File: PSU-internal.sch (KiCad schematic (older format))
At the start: 52 parts, among them Q3 BD241A

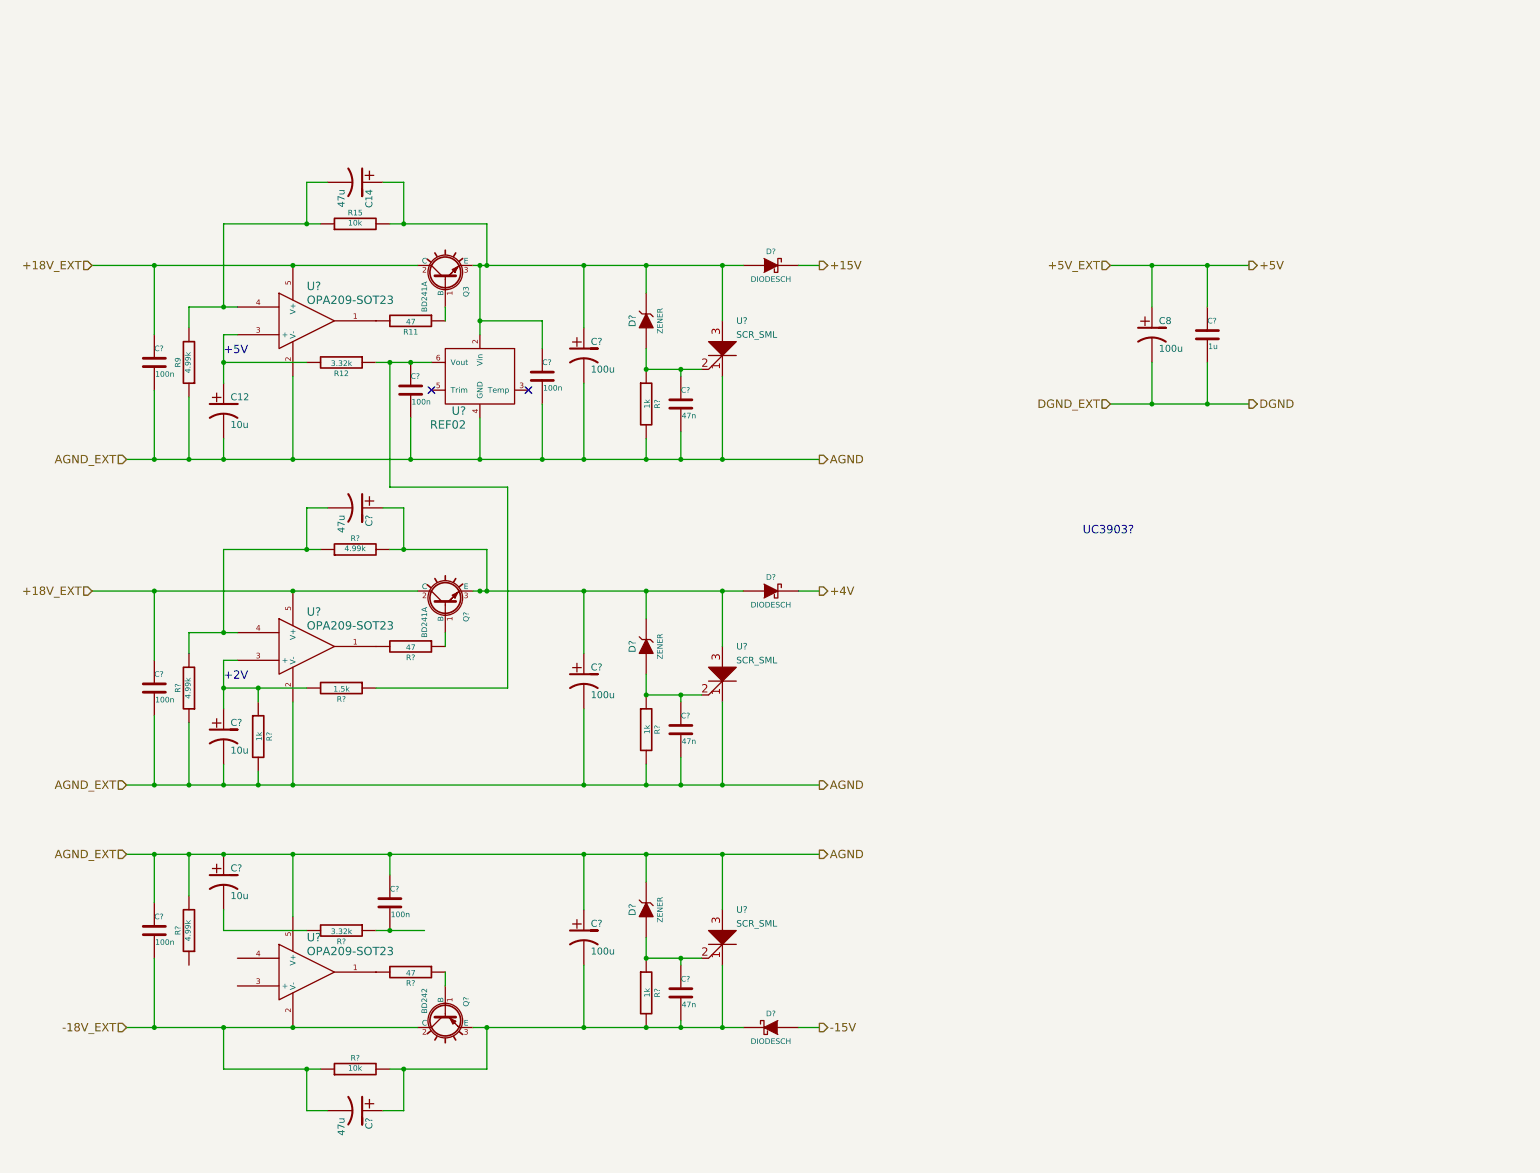
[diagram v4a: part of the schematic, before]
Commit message: Cleaned up the internal PSU a bit.
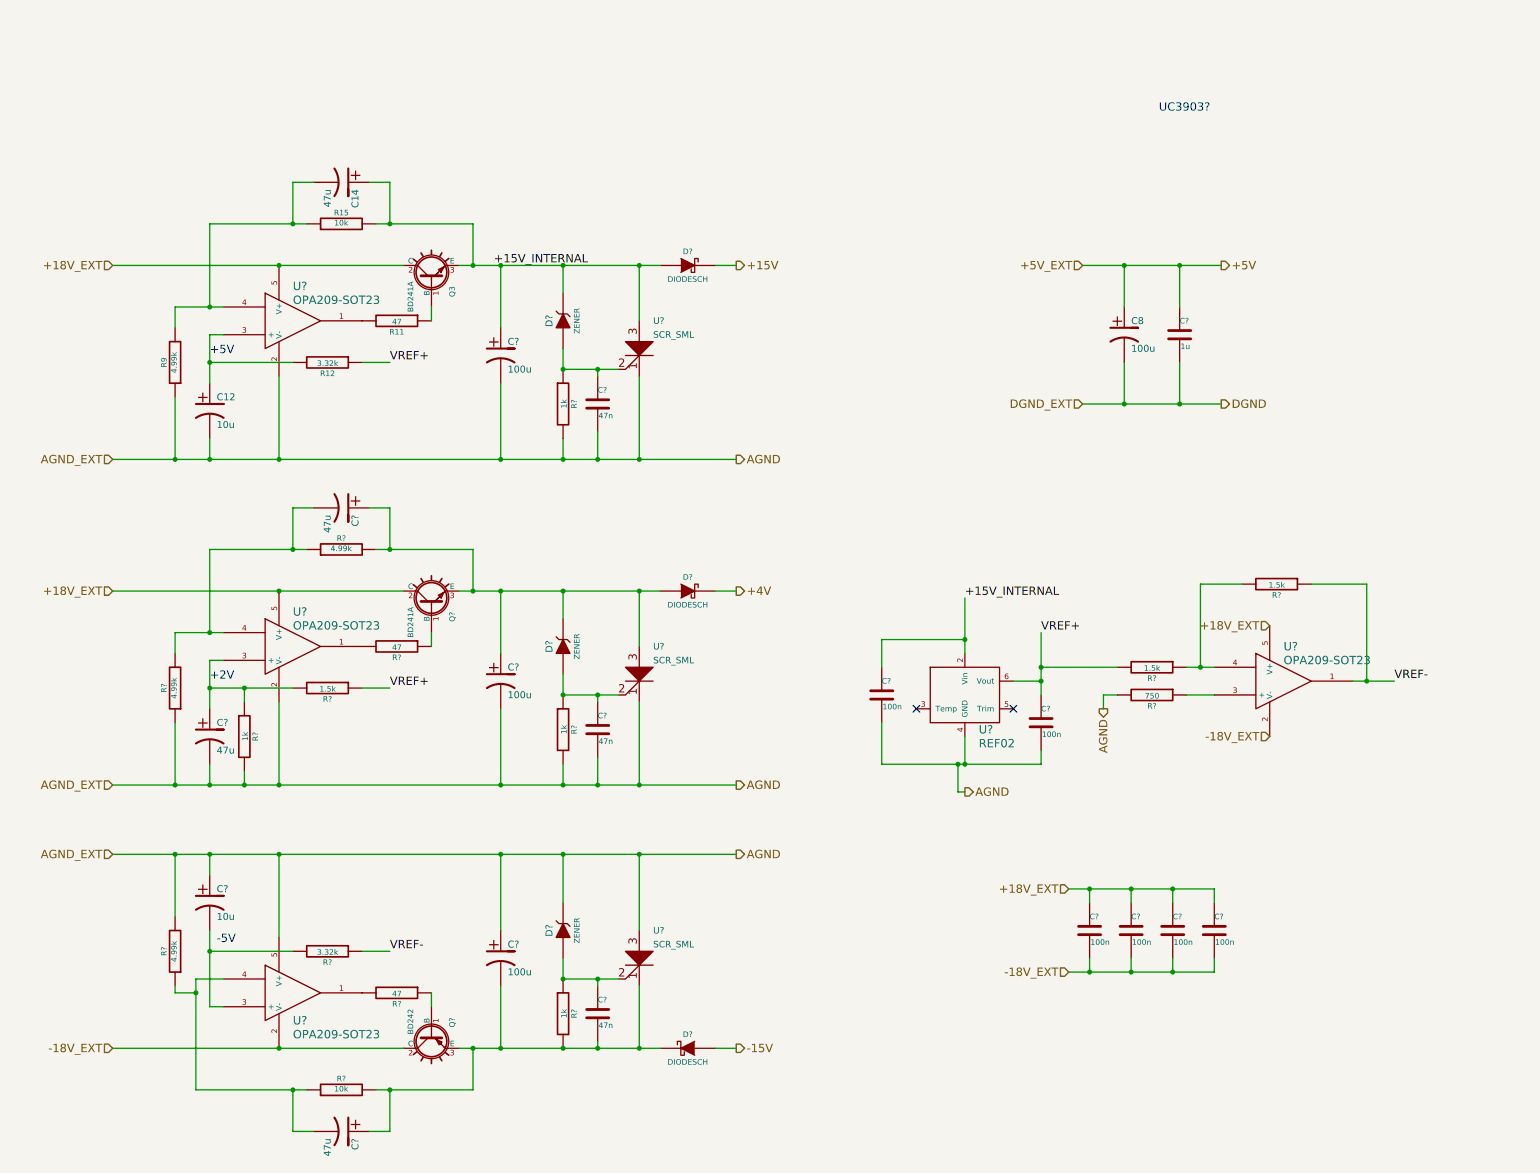
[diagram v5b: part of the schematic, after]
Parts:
- removed C? (x4): 100n, symbol C
- added C? (x4): 100n, symbol C
- added R? (x2): 1.5k, ~, symbol R
- added R?: 750, ~, symbol R
- added U?: OPA209-SOT23, symbol OPA209-SOT23
- C?: value 10u -> 47u
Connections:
- net +18V_EXT: now also C?.1, C?.1, C?.1, C?.1, U?.5 (V+)
- net -18V_EXT: now also C?.2, C?.2, C?.2, C?.2, U?.2 (V-); no longer C?.2, R?.1
- net AGND: now also R?.2
- net +15V_INTERNAL: now reaches C14.1, C?.1, C?.1, D?.1 (A), D?.2 (K), Q3.3 (E), R15.2, U?.2 (Vin), U?.3 (A)
- net VREF+: now reaches C?.1, R12.1, R?.1, U?.6 (Vout)
- net VREF+: now also R?.2
- net at U?.3 (+): now also C?.2, R?.2
- net at U?.4: now also C?.2, R?.1, R?.1
- net VREF-: now reaches R?.1
- net VREF-: now also R?.1, U?.1
- new net: R?.1, U?.3 (+)
- new net: R?.1, R?.2, U?.4
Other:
- note added: "-5V"
- moved on the sheet: C12, C14, C8, C?, D?, Q3, Q?, R11, R12, R15, R9, R?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

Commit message: Many additions; the system's almost together.  Just need to tidy up a few things around the PSU and the input stage.
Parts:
- removed D? (x3): DIODESCH, symbol DIODESCH
- removed U? (x2): SCR_SML, symbol SCR_SML
- added C?: 47n, symbol C
- added D?: 1N4734, symbol ZENER
- added R?: 1k, symbol R
- added U? (x3): 2N6507, TO-220AB, symbol SCR_SML
- D? (x2): value ZENER -> 1N4745
- D?: value ZENER -> 1N4731
- U?: value SCR_SML -> 2N6507; footprint (none) -> TO-220AB; DigiKey (none) -> 2N6507GOS-ND
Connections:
- net +15V: now also C14.1, C?.1, C?.1, D?.2 (K), Q3.3 (E), R15.2, U?.2 (Vin)
- net +18V_EXT: now also U?.3 (A), U?.3 (A)
- net +4V: now also C?.1, C?.1, D?.2 (K), Q?.3 (E), R?.2
- net +5V: now also U?.3 (A)
- net -15V: now also C?.1, C?.2, C?.2, Q?.3 (E), R?.2, R?.2
- net -18V_EXT: now also U?.1 (K)
- net AGND: now also U?.1 (K), U?.3 (A)
- net DGND: now also C?.2, U?.1 (K)
- net at C?.1, D?.1 (A), R?.1: now also U?.2 (G) (x2)
- removed net +15V_INTERNAL: C14.1, C?.1, C?.1, D?.2 (K), Q3.3 (E), R15.2, U?.2 (Vin), U?.3 (A)
- new net: C?.1, D?.1 (A), R?.1, U?.2 (G)
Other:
- note removed: "TODO:\n* Determine feedback cap value\n* Confirm selection of pass transistors\n* Heatsinking of regs and trans?\n* Schkotty and voltage drop"
- note removed: "UC3903?"
- moved on the sheet: C8, C?, R?, U?

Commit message: First complete system.  Still a few things to check.
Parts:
- removed C? (x5): 100n, symbol C
- removed C? (x3): 100u, symbol CP1
- removed C?: 1u, symbol C
- added C? (x5): 470n, symbol C
- added C? (x3): 470u, symbol CP1
- C8: value 100u -> 470u
- C?: value 100n -> 470n
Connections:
- net +15V: now also C?.1, C?.1
- net +18V_EXT: now also C?.1, C?.1, C?.1
- net +4V: now also C?.1
- net -15V: now also C?.2
- net -18V_EXT: now also C?.2, C?.2, C?.2
- net AGND: now also C?.1, C?.2, C?.2, C?.2, C?.2
- net VREF+: now also C?.1
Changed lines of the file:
@@
 LIBS:my-conn
 LIBS:ADC-cache
-EELAYER 24 0
+EELAYER 27 0
 EELAYER END
 $Descr A4 11693 8268
@@
 Sheet 2 6
 Title ""
-Date "12 may 2014"
+Date "21 may 2014"
 Rev ""
 Comp ""
@@
 P 7700 1800
 F 0 "C8" H 7750 1900 50  0000 L CNN
-F 1 "100u" H 7750 1700 50  0000 L CNN
+F 1 "470u" H 7750 1700 50  0000 L CNN
 F 2 "" H 7700 1800 60  0000 C CNN
 F 3 "" H 7700 1800 60  0000 C CNN
@@
 NoConn ~ 7800 4200
 NoConn ~ 7100 4200
-$Comp
-L C C?
-U 1 1 536453AA
-P 6850 4100
-F 0 "C?" H 6850 4200 40  0000 L CNN
-F 1 "100n" H 6856 4015 40  0000 L CNN
-F 2 "" H 6888 3950 30  0000 C CNN
-F 3 "" H 6850 4100 60  0000 C CNN
-	1    6850 4100
-	1    0    0    -1
-$EndComp
-$Comp
-L C C?
-U 1 1 536453B5
-P 8000 4300
-F 0 "C?" H 8000 4400 40  0000 L CNN
-F 1 "100n" H 8006 4215 40  0000 L CNN
-F 2 "" H 8038 4150 30  0000 C CNN
-F 3 "" H 8000 4300 60  0000 C CNN
-	1    8000 4300
-	1    0    0    -1
-$EndComp
-$Comp
-L CP1 C?
-U 1 1 53645A52
-P 4150 1950
-F 0 "C?" H 4200 2050 50  0000 L CNN
-F 1 "100u" H 4200 1850 50  0000 L CNN
-F 2 "" H 4150 1950 60  0000 C CNN
-F 3 "" H 4150 1950 60  0000 C CNN
-	1    4150 1950
-	1    0    0    -1
-$EndComp
 Text HLabel 7300 2300 0    60   Input ~ 0
 DGND_EXT
@@
 $EndComp
 $Comp
-L CP1 C?
-U 1 1 5368A6C9
-P 4150 6300
-F 0 "C?" H 4200 6400 50  0000 L CNN
-F 1 "100u" H 4200 6200 50  0000 L CNN
-F 2 "" H 4150 6300 60  0000 C CNN
-F 3 "" H 4150 6300 60  0000 C CNN
-	1    4150 6300
-	1    0    0    -1
-$EndComp
-$Comp
 L R R?
 U 1 1 5368A964
@@
 Text HLabel 9750 2300 2    60   Output ~ 0
 DGND
-$Comp
-L C C?
-U 1 1 53689541
-P 8100 1800
-F 0 "C?" H 8100 1900 40  0000 L CNN
-F 1 "1u" H 8106 1715 40  0000 L CNN
-F 2 "" H 8138 1650 30  0000 C CNN
-F 3 "" H 8100 1800 60  0000 C CNN
-	1    8100 1800
-	1    0    0    -1
-$EndComp
 Text HLabel 1350 1300 0    60   Input ~ 0
 +18V_EXT
@@
 F 3 "" H 2650 4050 60  0000 C CNN
 	1    2550 4050
-	1    0    0    -1
-$EndComp
-$Comp
-L CP1 C?
-U 1 1 536ECFEC
-P 4150 4300
-F 0 "C?" H 4200 4400 50  0000 L CNN
-F 1 "100u" H 4200 4200 50  0000 L CNN
-F 2 "" H 4150 4300 60  0000 C CNN
-F 3 "" H 4150 4300 60  0000 C CNN
-	1    4150 4300
 	1    0    0    -1
 $EndComp
@@
 P 8450 5750
 F 0 "C?" H 8450 5850 40  0000 L CNN
-F 1 "100n" H 8456 5665 40  0000 L CNN
+F 1 "470n" H 8456 5665 40  0000 L CNN
 F 2 "" H 8488 5600 30  0000 C CNN
 F 3 "" H 8450 5750 60  0000 C CNN
 F 4 "Bypass cap for OpAmp" H 8450 5750 60  0001 C CNN "Note"
 	1    8450 5750
-	1    0    0    -1
-$EndComp
-$Comp
-L C C?
-U 1 1 5370E202
-P 8750 5750
-F 0 "C?" H 8750 5850 40  0000 L CNN
-F 1 "100n" H 8756 5665 40  0000 L CNN
-F 2 "" H 8788 5600 30  0000 C CNN
-F 3 "" H 8750 5750 60  0000 C CNN
-F 4 "Bypass cap for OpAmp" H 8750 5750 60  0001 C CNN "Note"
-	1    8750 5750
-	1    0    0    -1
-$EndComp
-$Comp
-L C C?
-U 1 1 5370E209
-P 9050 5750
-F 0 "C?" H 9050 5850 40  0000 L CNN
-F 1 "100n" H 9056 5665 40  0000 L CNN
-F 2 "" H 9088 5600 30  0000 C CNN
-F 3 "" H 9050 5750 60  0000 C CNN
-F 4 "Bypass cap for OpAmp" H 9050 5750 60  0001 C CNN "Note"
-	1    9050 5750
-	1    0    0    -1
-$EndComp
-$Comp
-L C C?
-U 1 1 5370E210
-P 9350 5750
-F 0 "C?" H 9350 5850 40  0000 L CNN
-F 1 "100n" H 9356 5665 40  0000 L CNN
-F 2 "" H 9388 5600 30  0000 C CNN
-F 3 "" H 9350 5750 60  0000 C CNN
-F 4 "Bypass cap for OpAmp" H 9350 5750 60  0001 C CNN "Note"
-	1    9350 5750
 	1    0    0    -1
 $EndComp
@@
 Wire Wire Line
 	3850 6950 5850 6950
-Wire Wire Line
-	8100 1600 8100 1300
-Connection ~ 8100 1300
-Wire Wire Line
-	8100 2000 8100 2300
-Connection ~ 8100 2300
 Wire Wire Line
 	3650 6550 3650 6650
@@
 Wire Wire Line
 	8650 1700 8650 1800
+$Comp
+L C C?
+U 1 1 537C45A5
+P 8750 5750
+F 0 "C?" H 8750 5850 40  0000 L CNN
+F 1 "470n" H 8756 5665 40  0000 L CNN
+F 2 "" H 8788 5600 30  0000 C CNN
+F 3 "" H 8750 5750 60  0000 C CNN
+F 4 "Bypass cap for OpAmp" H 8750 5750 60  0001 C CNN "Note"
+	1    8750 5750
+	1    0    0    -1
+$EndComp
+$Comp
+L C C?
+U 1 1 537C45AC
+P 9050 5750
+F 0 "C?" H 9050 5850 40  0000 L CNN
+F 1 "470n" H 9056 5665 40  0000 L CNN
+F 2 "" H 9088 5600 30  0000 C CNN
+F 3 "" H 9050 5750 60  0000 C CNN
+F 4 "Bypass cap for OpAmp" H 9050 5750 60  0001 C CNN "Note"
+	1    9050 5750
+	1    0    0    -1
+$EndComp
+$Comp
+L C C?
+U 1 1 537C45B3
+P 9350 5750
+F 0 "C?" H 9350 5850 40  0000 L CNN
+F 1 "470n" H 9356 5665 40  0000 L CNN
+F 2 "" H 9388 5600 30  0000 C CNN
+F 3 "" H 9350 5750 60  0000 C CNN
+F 4 "Bypass cap for OpAmp" H 9350 5750 60  0001 C CNN "Note"
+	1    9350 5750
+	1    0    0    -1
+$EndComp
+$Comp
+L CP1 C?
+U 1 1 537C4758
+P 4150 1950
+F 0 "C?" H 4200 2050 50  0000 L CNN
+F 1 "470u" H 4200 1850 50  0000 L CNN
+F 2 "" H 4150 1950 60  0000 C CNN
+F 3 "" H 4150 1950 60  0000 C CNN
+	1    4150 1950
+	1    0    0    -1
+$EndComp
+$Comp
+L CP1 C?
+U 1 1 537C475E
+P 4150 4300
+F 0 "C?" H 4200 4400 50  0000 L CNN
+F 1 "470u" H 4200 4200 50  0000 L CNN
+F 2 "" H 4150 4300 60  0000 C CNN
+F 3 "" H 4150 4300 60  0000 C CNN
+	1    4150 4300
+	1    0    0    -1
+$EndComp
+$Comp
+L CP1 C?
+U 1 1 537C4764
+P 4150 6300
+F 0 "C?" H 4200 6400 50  0000 L CNN
+F 1 "470u" H 4200 6200 50  0000 L CNN
+F 2 "" H 4150 6300 60  0000 C CNN
+F 3 "" H 4150 6300 60  0000 C CNN
+	1    4150 6300
+	1    0    0    -1
+$EndComp
+$Comp
+L C C?
+U 1 1 537C48FE
+P 8000 4300
+F 0 "C?" H 8000 4400 40  0000 L CNN
+F 1 "470n" H 8006 4215 40  0000 L CNN
+F 2 "" H 8038 4150 30  0000 C CNN
+F 3 "" H 8000 4300 60  0000 C CNN
+F 4 "Bypass cap for OpAmp" H 8000 4300 60  0001 C CNN "Note"
+	1    8000 4300
+	1    0    0    -1
+$EndComp
+$Comp
+L C C?
+U 1 1 537C4905
+P 6850 4100
+F 0 "C?" H 6850 4200 40  0000 L CNN
+F 1 "470n" H 6856 4015 40  0000 L CNN
+F 2 "" H 6888 3950 30  0000 C CNN
+F 3 "" H 6850 4100 60  0000 C CNN
+F 4 "Bypass cap for OpAmp" H 6850 4100 60  0001 C CNN "Note"
+	1    6850 4100
+	1    0    0    -1
+$EndComp
 $EndSCHEMATC

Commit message: V1.0 Schematic Completed.
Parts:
- removed C? (x2): 47u, symbol CP1
- added C? (x2): 10u, symbol CP1
- C14: value 47u -> 10u; Type (none) -> Tantalum
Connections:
- net +4V: now also C?.1
- net -15V: now also C?.2
- net at R?.1, R?.1, U?.4: now also C?.1
- net at R?.1, R?.2, U?.4: now also C?.2
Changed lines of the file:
@@
 P 3000 700
 F 0 "C14" H 3050 800 50  0000 L CNN
-F 1 "47u" H 3050 600 50  0000 L CNN
+F 1 "10u" H 3050 600 50  0000 L CNN
 F 2 "" H 3000 700 60  0000 C CNN
 F 3 "" H 3000 700 60  0000 C CNN
+F 4 "Tantalum" H 3000 700 60  0001 C CNN "Type"
 	1    3000 700
 	0    1    1    0
@@
 	1    3000 7250
 	0    -1   -1   0
-$EndComp
-$Comp
-L CP1 C?
-U 1 1 5368A222
-P 3000 7550
-F 0 "C?" H 3050 7650 50  0000 L CNN
-F 1 "47u" H 3050 7450 50  0000 L CNN
-F 2 "" H 3000 7550 60  0000 C CNN
-F 3 "" H 3000 7550 60  0000 C CNN
-	1    3000 7550
-	0    1    1    0
 $EndComp
 $Comp
@@
 	1    3000 3350
 	0    -1   -1   0
-$EndComp
-$Comp
-L CP1 C?
-U 1 1 536ECFBF
-P 3000 3050
-F 0 "C?" H 3050 3150 50  0000 L CNN
-F 1 "47u" H 3050 2950 50  0000 L CNN
-F 2 "" H 3000 3050 60  0000 C CNN
-F 3 "" H 3000 3050 60  0000 C CNN
-	1    3000 3050
-	0    1    1    0
 $EndComp
 $Comp
@@
 	1    0    0    -1
 $EndComp
+$Comp
+L CP1 C?
+U 1 1 537CC00D
+P 3000 3050
+F 0 "C?" H 3050 3150 50  0000 L CNN
+F 1 "10u" H 3050 2950 50  0000 L CNN
+F 2 "" H 3000 3050 60  0000 C CNN
+F 3 "" H 3000 3050 60  0000 C CNN
+F 4 "Tantalum" H 3000 3050 60  0001 C CNN "Type"
+	1    3000 3050
+	0    1    1    0
+$EndComp
+$Comp
+L CP1 C?
+U 1 1 537CC020
+P 3000 7550
+F 0 "C?" H 3050 7650 50  0000 L CNN
+F 1 "10u" H 3050 7450 50  0000 L CNN
+F 2 "" H 3000 7550 60  0000 C CNN
+F 3 "" H 3000 7550 60  0000 C CNN
+F 4 "Tantalum" H 3000 7550 60  0001 C CNN "Type"
+	1    3000 7550
+	0    -1   -1   0
+$EndComp
 $EndSCHEMATC
